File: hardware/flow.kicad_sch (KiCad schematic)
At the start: 0 parts

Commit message: Flow module completed
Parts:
- added R?: 4K7, symbol Device:R_Small
- added R?: 1K, symbol Device:R_Small
- added U?: 4N25, Package_DIP:DIP-6_W7.62mm, symbol Isolator:4N25
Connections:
- new net: R?.2, U?.1
- new net +3V3: R?.1
- new net FLOW: R?.2, U?.5
- new net FLOW_IN: R?.1
- new net GND: U?.2, U?.4
- no-connect marks 0 -> 1
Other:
- note added: "12V = 1K 5V = 220R"
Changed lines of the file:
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@@
 (kicad_sch (version 20211123) (generator eeschema)
   (paper "A4")
+  (junction (at 155.575 97.79) (diameter 0) (color 0 0 0 0)
+  )
+  (no_connect (at 153.035 95.25))
+  (wire (pts (xy 155.575 88.265) (xy 155.575 90.17))
+    (stroke (width 0) (type default) (color 0 0 0 0))
+  )
+  (wire (pts (xy 127 95.25) (xy 129.54 95.25))
+    (stroke (width 0) (type default) (color 0 0 0 0))
+  )
+  (wire (pts (xy 153.035 100.33) (xy 155.575 100.33))
+    (stroke (width 0) (type default) (color 0 0 0 0))
+  )
+  (wire (pts (xy 155.575 95.25) (xy 155.575 97.79))
+    (stroke (width 0) (type default) (color 0 0 0 0))
+  )
+  (wire (pts (xy 155.575 97.79) (xy 153.035 97.79))
+    (stroke (width 0) (type default) (color 0 0 0 0))
+  )
+  (wire (pts (xy 160.02 97.79) (xy 155.575 97.79))
+    (stroke (width 0) (type default) (color 0 0 0 0))
+  )
+  (wire (pts (xy 134.62 95.25) (xy 137.795 95.25))
+    (stroke (width 0) (type default) (color 0 0 0 0))
+  )
+  (wire (pts (xy 155.575 100.33) (xy 155.575 102.235))
+    (stroke (width 0) (type default) (color 0 0 0 0))
+  )
+  (wire (pts (xy 135.89 100.33) (xy 137.795 100.33))
+    (stroke (width 0) (type default) (color 0 0 0 0))
+  )
+  (wire (pts (xy 135.89 102.235) (xy 135.89 100.33))
+    (stroke (width 0) (type default) (color 0 0 0 0))
+  )
+  (text "12V = 1K\n5V = 220R" (at 126.365 90.805 0)
+    (effects (font (size 1.27 1.27)) (justify left bottom))
+  )
+  (global_label "FLOW_IN" (shape input) (at 127 95.25 180) (fields_autoplaced)
+    (effects (font (size 1.27 1.27)) (justify right))
+    (property "Intersheet References" "${INTERSHEET_REFS}" (id 0) (at 116.7855 95.1706 0)
+      (effects (font (size 1.27 1.27)) (justify right) hide)
+    )
+  )
+  (global_label "FLOW" (shape input) (at 160.02 97.79 0) (fields_autoplaced)
+    (effects (font (size 1.27 1.27)) (justify left))
+    (property "Intersheet References" "${INTERSHEET_REFS}" (id 0) (at 167.3317 97.7106 0)
+      (effects (font (size 1.27 1.27)) (justify left) hide)
+    )
+  )
+  (symbol (lib_id "power:GND") (at 135.89 102.235 0) (unit 1)
+    (in_bom yes) (on_board yes) (fields_autoplaced)
+    (property "Reference" "#PWR?" (id 0) (at 135.89 108.585 0)
+      (effects (font (size 1.27 1.27)) hide)
+    )
+    (property "Value" "GND" (id 1) (at 135.89 106.68 0))
+    (property "Footprint" "" (id 2) (at 135.89 102.235 0)
+      (effects (font (size 1.27 1.27)) hide)
+    )
+    (property "Datasheet" "" (id 3) (at 135.89 102.235 0)
+      (effects (font (size 1.27 1.27)) hide)
+    )
+    (pin "1")
+  )
+  (symbol (lib_id "Isolator:4N25") (at 145.415 97.79 0) (unit 1)
+    (in_bom yes) (on_board yes)
+    (property "Reference" "U?" (id 0) (at 145.415 92.71 0))
+    (property "Value" "4N25" (id 1) (at 145.415 102.87 0))
+    (property "Footprint" "Package_DIP:DIP-6_W7.62mm" (id 2) (at 140.335 102.87 0)
+      (effects (font (size 1.27 1.27) italic) (justify left) hide)
+    )
+    (property "Datasheet" "https://www.vishay.com/docs/83725/4n25.pdf" (id 3) (at 145.415 97.79 0)
+      (effects (font (size 1.27 1.27)) (justify left) hide)
+    )
+    (pin "1")
+    (pin "2")
+    (pin "3")
+    (pin "4")
+    (pin "5")
+    (pin "6")
+  )
+  (symbol (lib_id "power:+3V3") (at 155.575 88.265 0) (unit 1)
+    (in_bom yes) (on_board yes) (fields_autoplaced)
+    (property "Reference" "#PWR?" (id 0) (at 155.575 92.075 0)
+      (effects (font (size 1.27 1.27)) hide)
+    )
+    (property "Value" "+3V3" (id 1) (at 155.575 82.55 0))
+    (property "Footprint" "" (id 2) (at 155.575 88.265 0)
+      (effects (font (size 1.27 1.27)) hide)
+    )
+    (property "Datasheet" "" (id 3) (at 155.575 88.265 0)
+      (effects (font (size 1.27 1.27)) hide)
+    )
+    (pin "1")
+  )
+  (symbol (lib_id "Device:R_Small") (at 155.575 92.71 0) (unit 1)
+    (in_bom yes) (on_board yes) (fields_autoplaced)
+    (property "Reference" "R?" (id 0) (at 158.115 91.4399 0)
+      (effects (font (size 1.27 1.27)) (justify left))
+    )
+    (property "Value" "4K7" (id 1) (at 158.115 93.9799 0)
+      (effects (font (size 1.27 1.27)) (justify left))
+    )
+    (property "Footprint" "" (id 2) (at 155.575 92.71 0)
+      (effects (font (size 1.27 1.27)) hide)
+    )
+    (property "Datasheet" "~" (id 3) (at 155.575 92.71 0)
+      (effects (font (size 1.27 1.27)) hide)
+    )
+    (pin "1")
+    (pin "2")
+  )
+  (symbol (lib_id "Device:R_Small") (at 132.08 95.25 90) (unit 1)
+    (in_bom yes) (on_board yes)
+    (property "Reference" "R?" (id 0) (at 132.08 92.71 90))
+    (property "Value" "1K" (id 1) (at 132.08 97.155 90))
+    (property "Footprint" "" (id 2) (at 132.08 95.25 0)
+      (effects (font (size 1.27 1.27)) hide)
+    )
+    (property "Datasheet" "~" (id 3) (at 132.08 95.25 0)
+      (effects (font (size 1.27 1.27)) hide)
+    )
+    (pin "1")
+    (pin "2")
+  )
+  (symbol (lib_id "power:GND") (at 155.575 102.235 0) (unit 1)
+    (in_bom yes) (on_board yes) (fields_autoplaced)
+    (property "Reference" "#PWR?" (id 0) (at 155.575 108.585 0)
+      (effects (font (size 1.27 1.27)) hide)
+    )
+    (property "Value" "GND" (id 1) (at 155.575 106.68 0))
+    (property "Footprint" "" (id 2) (at 155.575 102.235 0)
+      (effects (font (size 1.27 1.27)) hide)
+    )
+    (property "Datasheet" "" (id 3) (at 155.575 102.235 0)
+      (effects (font (size 1.27 1.27)) hide)
+    )
+    (pin "1")
+  )
 )

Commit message: Schematics are completed
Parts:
- R4, R5: renamed from R?; footprint (none) -> Resistor_SMD:R_0603_1608Metric
- gave numbers to parts that had none: 1
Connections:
- net FLOW_IN renamed FLOW_SENSOR
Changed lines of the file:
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@@
     (effects (font (size 1.27 1.27)) (justify left bottom))
-  )
-  (global_label "FLOW_IN" (shape input) (at 127 95.25 180) (fields_autoplaced)
-    (effects (font (size 1.27 1.27)) (justify right))
-    (property "Intersheet References" "${INTERSHEET_REFS}" (id 0) (at 116.7855 95.1706 0)
-      (effects (font (size 1.27 1.27)) (justify right) hide)
-    )
   )
   (global_label "FLOW" (shape input) (at 160.02 97.79 0) (fields_autoplaced)
@@
     )
   )
+  (hierarchical_label "FLOW_SENSOR" (shape input) (at 127 95.25 180)
+    (effects (font (size 1.27 1.27)) (justify right))
+  )
   (symbol (lib_id "power:GND") (at 135.89 102.235 0) (unit 1)
     (in_bom yes) (on_board yes) (fields_autoplaced)
-    (property "Reference" "#PWR?" (id 0) (at 135.89 108.585 0)
+    (property "Reference" "#PWR016" (id 0) (at 135.89 108.585 0)
       (effects (font (size 1.27 1.27)) hide)
     )
@@
   (symbol (lib_id "Isolator:4N25") (at 145.415 97.79 0) (unit 1)
     (in_bom yes) (on_board yes)
-    (property "Reference" "U?" (id 0) (at 145.415 92.71 0))
+    (property "Reference" "U2" (id 0) (at 145.415 92.71 0))
     (property "Value" "4N25" (id 1) (at 145.415 102.87 0))
     (property "Footprint" "Package_DIP:DIP-6_W7.62mm" (id 2) (at 140.335 102.87 0)
@@
   (symbol (lib_id "power:+3V3") (at 155.575 88.265 0) (unit 1)
     (in_bom yes) (on_board yes) (fields_autoplaced)
-    (property "Reference" "#PWR?" (id 0) (at 155.575 92.075 0)
+    (property "Reference" "#PWR017" (id 0) (at 155.575 92.075 0)
       (effects (font (size 1.27 1.27)) hide)
     )
@@
   (symbol (lib_id "Device:R_Small") (at 155.575 92.71 0) (unit 1)
     (in_bom yes) (on_board yes) (fields_autoplaced)
-    (property "Reference" "R?" (id 0) (at 158.115 91.4399 0)
+    (property "Reference" "R5" (id 0) (at 158.115 91.4399 0)
       (effects (font (size 1.27 1.27)) (justify left))
     )
@@
       (effects (font (size 1.27 1.27)) (justify left))
     )
-    (property "Footprint" "" (id 2) (at 155.575 92.71 0)
+    (property "Footprint" "Resistor_SMD:R_0603_1608Metric" (id 2) (at 155.575 92.71 0)
       (effects (font (size 1.27 1.27)) hide)
     )
@@
   (symbol (lib_id "Device:R_Small") (at 132.08 95.25 90) (unit 1)
     (in_bom yes) (on_board yes)
-    (property "Reference" "R?" (id 0) (at 132.08 92.71 90))
+    (property "Reference" "R4" (id 0) (at 132.08 92.71 90))
     (property "Value" "1K" (id 1) (at 132.08 97.155 90))
-    (property "Footprint" "" (id 2) (at 132.08 95.25 0)
+    (property "Footprint" "Resistor_SMD:R_0603_1608Metric" (id 2) (at 132.08 95.25 0)
       (effects (font (size 1.27 1.27)) hide)
     )
@@
   (symbol (lib_id "power:GND") (at 155.575 102.235 0) (unit 1)
     (in_bom yes) (on_board yes) (fields_autoplaced)
-    (property "Reference" "#PWR?" (id 0) (at 155.575 108.585 0)
+    (property "Reference" "#PWR018" (id 0) (at 155.575 108.585 0)
       (effects (font (size 1.27 1.27)) hide)
     )

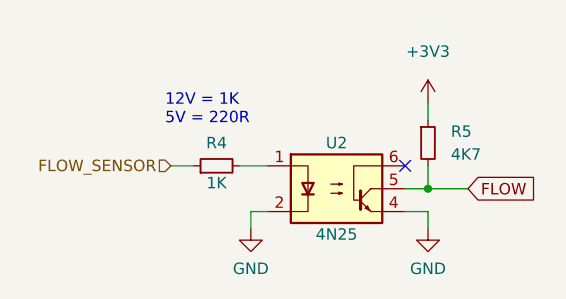
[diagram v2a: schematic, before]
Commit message: Footprints are assigned and Cut edges fixed
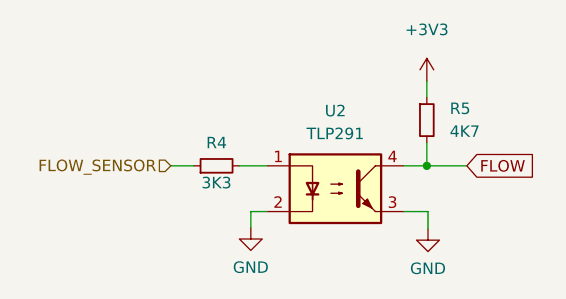
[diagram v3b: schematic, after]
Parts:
- removed U2: 4N25, Package_DIP:DIP-6_W7.62mm, symbol Isolator:4N25
- added U2: TLP291, Package_SO:SOIC-4_4.55x2.6mm_P1.27mm, symbol Isolator:TLP291
- R4: value 1K -> 3K3
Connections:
- net FLOW: now also U2.4
- net GND: now also U2.2, U2.3
- net at R4.2: now also U2.1
- no-connect marks 1 -> 0
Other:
- note removed: "12V = 1K 5V = 220R"
- moved on the sheet: R5
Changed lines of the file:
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@@
 (kicad_sch (version 20211123) (generator eeschema)
   (paper "A4")
-  (junction (at 155.575 97.79) (diameter 0) (color 0 0 0 0)
+  (junction (at 155.448 95.25) (diameter 0) (color 0 0 0 0)
   )
-  (no_connect (at 153.035 95.25))
-  (wire (pts (xy 155.575 88.265) (xy 155.575 90.17))
+  (wire (pts (xy 135.89 100.33) (xy 137.668 100.33))
+    (stroke (width 0) (type default) (color 0 0 0 0))
+  )
+  (wire (pts (xy 135.89 102.108) (xy 135.89 100.33))
     (stroke (width 0) (type default) (color 0 0 0 0))
   )
@@
     (stroke (width 0) (type default) (color 0 0 0 0))
   )
-  (wire (pts (xy 153.035 100.33) (xy 155.575 100.33))
+  (wire (pts (xy 152.908 100.33) (xy 155.575 100.33))
     (stroke (width 0) (type default) (color 0 0 0 0))
   )
-  (wire (pts (xy 155.575 95.25) (xy 155.575 97.79))
+  (wire (pts (xy 155.448 85.852) (xy 155.448 87.63))
     (stroke (width 0) (type default) (color 0 0 0 0))
   )
-  (wire (pts (xy 155.575 97.79) (xy 153.035 97.79))
+  (wire (pts (xy 155.448 92.71) (xy 155.448 95.25))
     (stroke (width 0) (type default) (color 0 0 0 0))
   )
-  (wire (pts (xy 160.02 97.79) (xy 155.575 97.79))
+  (wire (pts (xy 155.448 95.25) (xy 152.908 95.25))
     (stroke (width 0) (type default) (color 0 0 0 0))
   )
-  (wire (pts (xy 134.62 95.25) (xy 137.795 95.25))
+  (wire (pts (xy 159.893 95.25) (xy 155.448 95.25))
+    (stroke (width 0) (type default) (color 0 0 0 0))
+  )
+  (wire (pts (xy 134.62 95.25) (xy 137.668 95.25))
     (stroke (width 0) (type default) (color 0 0 0 0))
   )
@@
     (stroke (width 0) (type default) (color 0 0 0 0))
   )
-  (wire (pts (xy 135.89 100.33) (xy 137.795 100.33))
-    (stroke (width 0) (type default) (color 0 0 0 0))
-  )
-  (wire (pts (xy 135.89 102.235) (xy 135.89 100.33))
-    (stroke (width 0) (type default) (color 0 0 0 0))
-  )
-  (text "12V = 1K\n5V = 220R" (at 126.365 90.805 0)
-    (effects (font (size 1.27 1.27)) (justify left bottom))
-  )
-  (global_label "FLOW" (shape input) (at 160.02 97.79 0) (fields_autoplaced)
+  (global_label "FLOW" (shape input) (at 159.893 95.25 0) (fields_autoplaced)
     (effects (font (size 1.27 1.27)) (justify left))
-    (property "Intersheet References" "${INTERSHEET_REFS}" (id 0) (at 167.3317 97.7106 0)
+    (property "Intersheet References" "${INTERSHEET_REFS}" (id 0) (at 167.2047 95.1706 0)
       (effects (font (size 1.27 1.27)) (justify left) hide)
     )
@@
     (effects (font (size 1.27 1.27)) (justify right))
   )
-  (symbol (lib_id "power:GND") (at 135.89 102.235 0) (unit 1)
+  (symbol (lib_id "power:GND") (at 135.89 102.108 0) (unit 1)
     (in_bom yes) (on_board yes) (fields_autoplaced)
-    (property "Reference" "#PWR016" (id 0) (at 135.89 108.585 0)
+    (property "Reference" "#PWR016" (id 0) (at 135.89 108.458 0)
       (effects (font (size 1.27 1.27)) hide)
     )
-    (property "Value" "GND" (id 1) (at 135.89 106.68 0))
-    (property "Footprint" "" (id 2) (at 135.89 102.235 0)
+    (property "Value" "GND" (id 1) (at 135.89 106.553 0))
+    (property "Footprint" "" (id 2) (at 135.89 102.108 0)
       (effects (font (size 1.27 1.27)) hide)
     )
-    (property "Datasheet" "" (id 3) (at 135.89 102.235 0)
+    (property "Datasheet" "" (id 3) (at 135.89 102.108 0)
       (effects (font (size 1.27 1.27)) hide)
     )
     (pin "1")
   )
-  (symbol (lib_id "Isolator:4N25") (at 145.415 97.79 0) (unit 1)
-    (in_bom yes) (on_board yes)
-    (property "Reference" "U2" (id 0) (at 145.415 92.71 0))
-    (property "Value" "4N25" (id 1) (at 145.415 102.87 0))
-    (property "Footprint" "Package_DIP:DIP-6_W7.62mm" (id 2) (at 140.335 102.87 0)
-      (effects (font (size 1.27 1.27) italic) (justify left) hide)
-    )
-    (property "Datasheet" "https://www.vishay.com/docs/83725/4n25.pdf" (id 3) (at 145.415 97.79 0)
-      (effects (font (size 1.27 1.27)) (justify left) hide)
-    )
-    (pin "1")
-    (pin "2")
-    (pin "3")
-    (pin "4")
-    (pin "5")
-    (pin "6")
-  )
-  (symbol (lib_id "power:+3V3") (at 155.575 88.265 0) (unit 1)
+  (symbol (lib_id "power:+3V3") (at 155.448 85.852 0) (unit 1)
     (in_bom yes) (on_board yes) (fields_autoplaced)
-    (property "Reference" "#PWR017" (id 0) (at 155.575 92.075 0)
+    (property "Reference" "#PWR017" (id 0) (at 155.448 89.662 0)
       (effects (font (size 1.27 1.27)) hide)
     )
-    (property "Value" "+3V3" (id 1) (at 155.575 82.55 0))
-    (property "Footprint" "" (id 2) (at 155.575 88.265 0)
+    (property "Value" "+3V3" (id 1) (at 155.448 80.137 0))
+    (property "Footprint" "" (id 2) (at 155.448 85.852 0)
       (effects (font (size 1.27 1.27)) hide)
     )
-    (property "Datasheet" "" (id 3) (at 155.575 88.265 0)
+    (property "Datasheet" "" (id 3) (at 155.448 85.852 0)
       (effects (font (size 1.27 1.27)) hide)
     )
     (pin "1")
   )
-  (symbol (lib_id "Device:R_Small") (at 155.575 92.71 0) (unit 1)
+  (symbol (lib_id "Device:R_Small") (at 155.448 90.17 0) (unit 1)
     (in_bom yes) (on_board yes) (fields_autoplaced)
-    (property "Reference" "R5" (id 0) (at 158.115 91.4399 0)
+    (property "Reference" "R5" (id 0) (at 157.988 88.8999 0)
       (effects (font (size 1.27 1.27)) (justify left))
     )
-    (property "Value" "4K7" (id 1) (at 158.115 93.9799 0)
+    (property "Value" "4K7" (id 1) (at 157.988 91.4399 0)
       (effects (font (size 1.27 1.27)) (justify left))
     )
-    (property "Footprint" "Resistor_SMD:R_0603_1608Metric" (id 2) (at 155.575 92.71 0)
+    (property "Footprint" "Resistor_SMD:R_0603_1608Metric" (id 2) (at 155.448 90.17 0)
       (effects (font (size 1.27 1.27)) hide)
     )
-    (property "Datasheet" "~" (id 3) (at 155.575 92.71 0)
+    (property "Datasheet" "~" (id 3) (at 155.448 90.17 0)
       (effects (font (size 1.27 1.27)) hide)
     )
@@
     (in_bom yes) (on_board yes)
     (property "Reference" "R4" (id 0) (at 132.08 92.71 90))
-    (property "Value" "1K" (id 1) (at 132.08 97.155 90))
+    (property "Value" "3K3" (id 1) (at 132.08 97.155 90))
     (property "Footprint" "Resistor_SMD:R_0603_1608Metric" (id 2) (at 132.08 95.25 0)
       (effects (font (size 1.27 1.27)) hide)
@@
     (pin "2")
   )
+  (symbol (lib_id "Isolator:TLP291") (at 145.288 97.79 0) (unit 1)
+    (in_bom yes) (on_board yes) (fields_autoplaced)
+    (property "Reference" "U2" (id 0) (at 145.288 89.154 0))
+    (property "Value" "TLP291" (id 1) (at 145.288 91.694 0))
+    (property "Footprint" "Package_SO:SOIC-4_4.55x2.6mm_P1.27mm" (id 2) (at 140.208 102.87 0)
+      (effects (font (size 1.27 1.27) italic) (justify left) hide)
+    )
+    (property "Datasheet" "https://toshiba.semicon-storage.com/info/docget.jsp?did=12884&prodName=TLP291" (id 3) (at 145.288 97.79 0)
+      (effects (font (size 1.27 1.27)) (justify left) hide)
+    )
+    (pin "1")
+    (pin "2")
+    (pin "3")
+    (pin "4")
+  )
   (symbol (lib_id "power:GND") (at 155.575 102.235 0) (unit 1)
